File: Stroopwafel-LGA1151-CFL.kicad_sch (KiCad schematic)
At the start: 0 parts

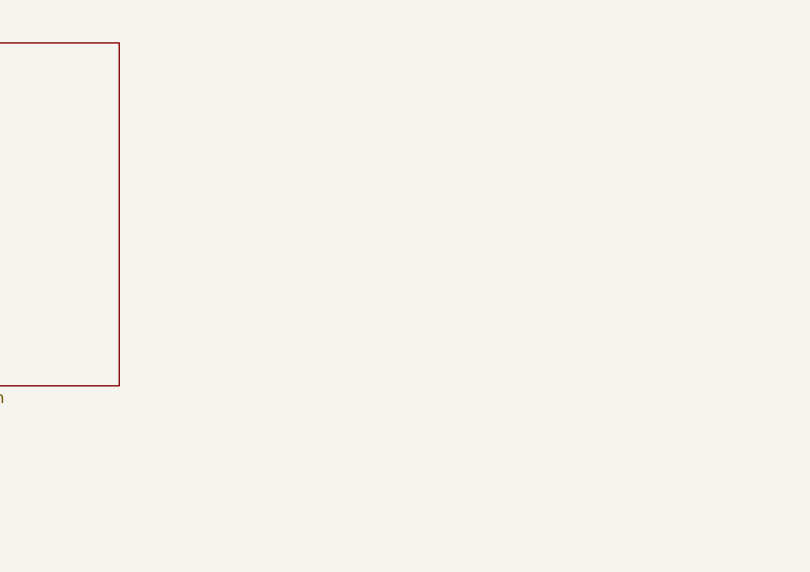
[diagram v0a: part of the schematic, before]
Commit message: Added CPU DDI symbol
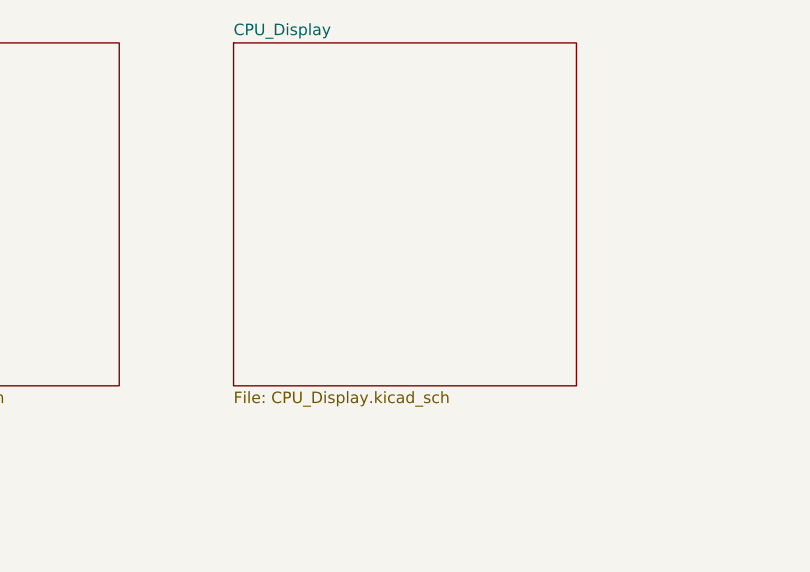
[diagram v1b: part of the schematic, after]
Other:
- added sheet CPU_Display (CPU_Display.kicad_sch)
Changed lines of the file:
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@@
+		)
+	)
+	(sheet
+		(at 177.8 76.2)
+		(size 38.1 38.1)
+		(exclude_from_sim no)
+		(in_bom yes)
+		(on_board yes)
+		(dnp no)
+		(fields_autoplaced yes)
+		(stroke
+			(width 0.1524)
+			(type solid)
+		)
+		(fill
+			(color 0 0 0 0.0000)
+		)
+		(property "Sheetname" "CPU_Display"
+			(at 177.8 75.4884 0)
+			(effects
+				(font
+					(size 1.27 1.27)
+				)
+				(justify left bottom)
+			)
+		)
+		(property "Sheetfile" "CPU_Display.kicad_sch"
+			(at 177.8 114.8846 0)
+			(effects
+				(font
+					(size 1.27 1.27)
+				)
+				(justify left top)
+			)
+		)
+		(instances
+			(project "Stroopwafel-LGA1151-CFL"
+				(path "/4bc771b8-eb19-46d0-8798-27231a7c6e83"
+					(page "4")
+				)
+			)
 		)
 	)

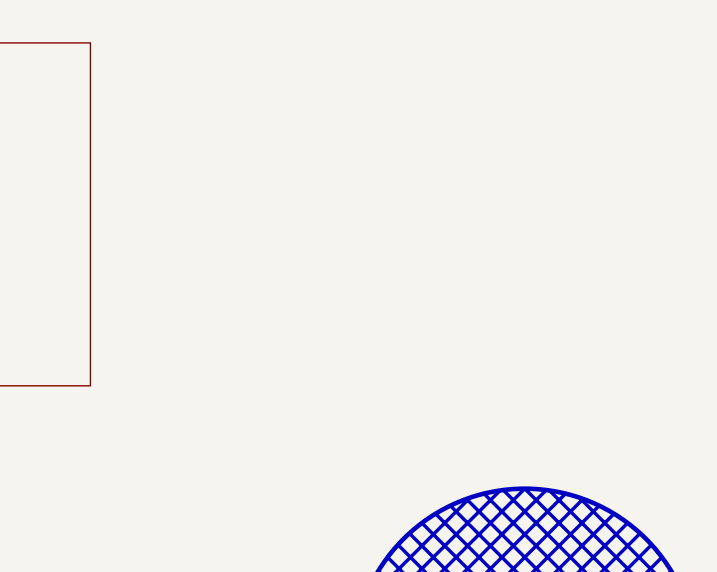
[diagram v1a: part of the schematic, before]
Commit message: Added CPU clock/cfg/vid/jtag symbol
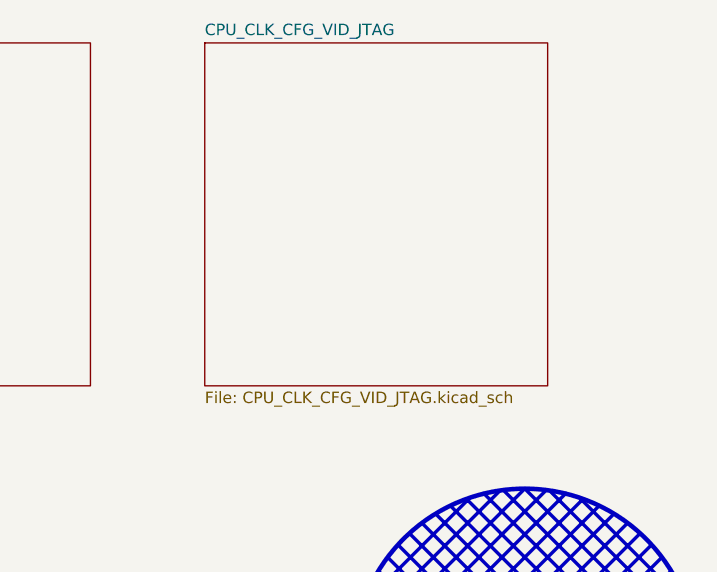
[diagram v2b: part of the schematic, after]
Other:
- added sheet CPU_CLK_CFG_VID_JTAG (CPU_CLK_CFG_VID_JTAG.kicad_sch)
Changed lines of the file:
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@@
+	)
+	(sheet
+		(at 228.6 76.2)
+		(size 38.1 38.1)
+		(exclude_from_sim no)
+		(in_bom yes)
+		(on_board yes)
+		(dnp no)
+		(fields_autoplaced yes)
+		(stroke
+			(width 0.1524)
+			(type solid)
+		)
+		(fill
+			(color 0 0 0 0.0000)
+		)
+		(property "Sheetname" "CPU_CLK_CFG_VID_JTAG"
+			(at 228.6 75.4884 0)
+			(effects
+				(font
+					(size 1.27 1.27)
+				)
+				(justify left bottom)
+			)
+		)
+		(property "Sheetfile" "CPU_CLK_CFG_VID_JTAG.kicad_sch"
+			(at 228.6 114.8846 0)
+			(effects
+				(font
+					(size 1.27 1.27)
+				)
+				(justify left top)
+			)
+		)
+		(instances
+			(project "Stroopwafel-LGA1151-CFL"
+				(path "/4bc771b8-eb19-46d0-8798-27231a7c6e83"
+					(page "5")
+				)
+			)
+		)
 	)
 	(sheet

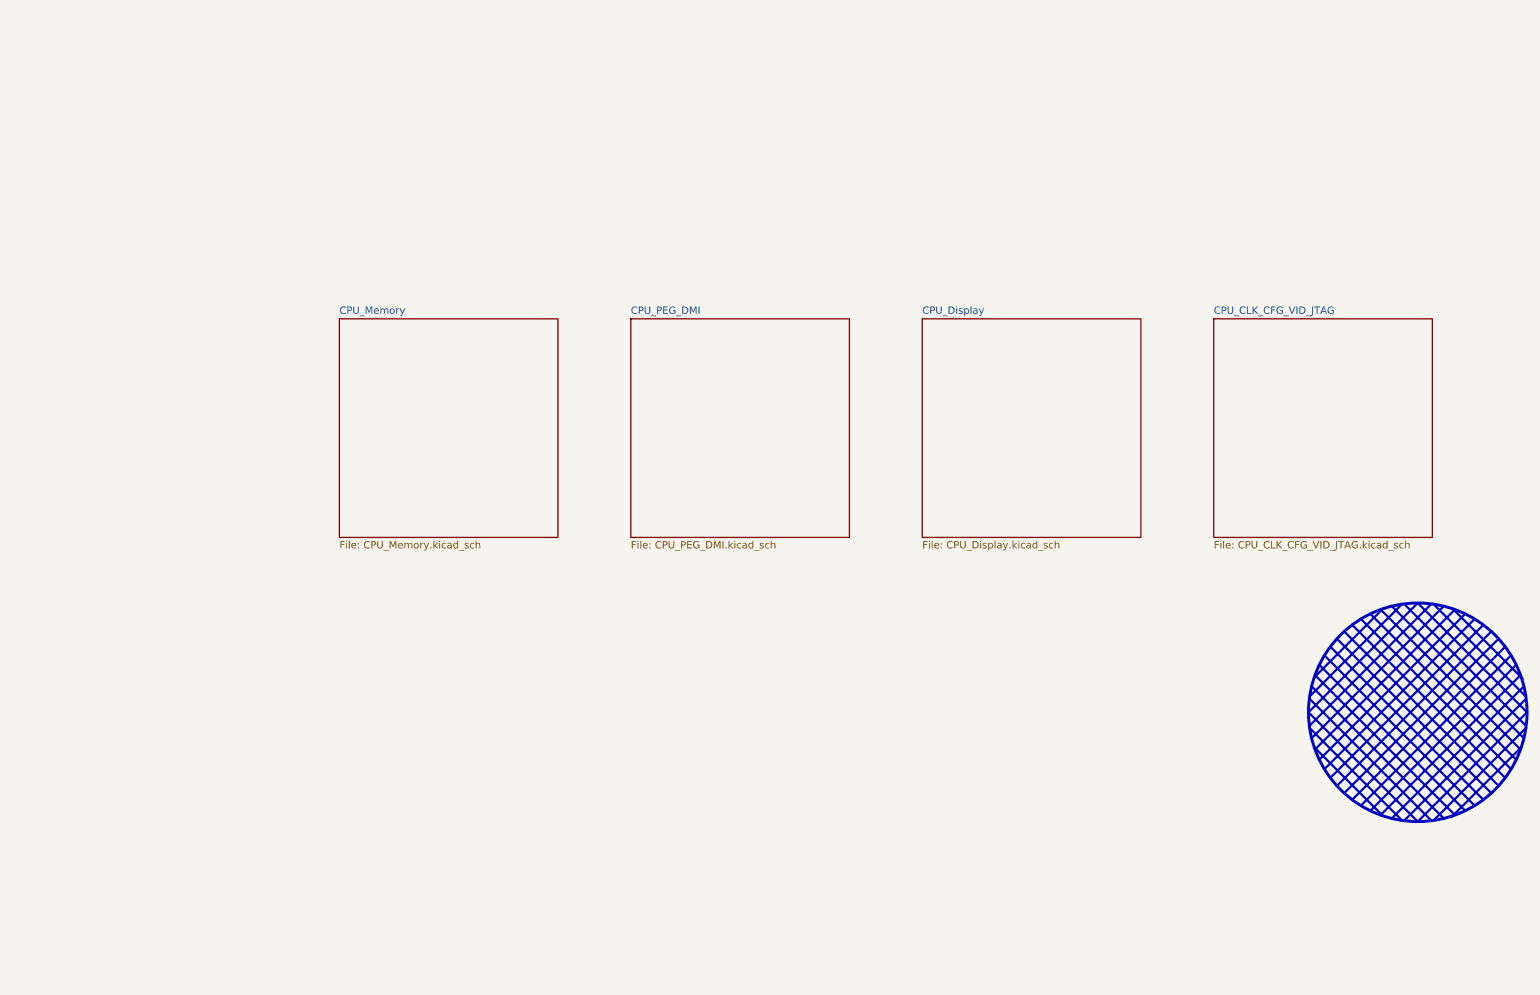
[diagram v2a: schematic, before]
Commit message: Added CPU GND and Core VCC symbols
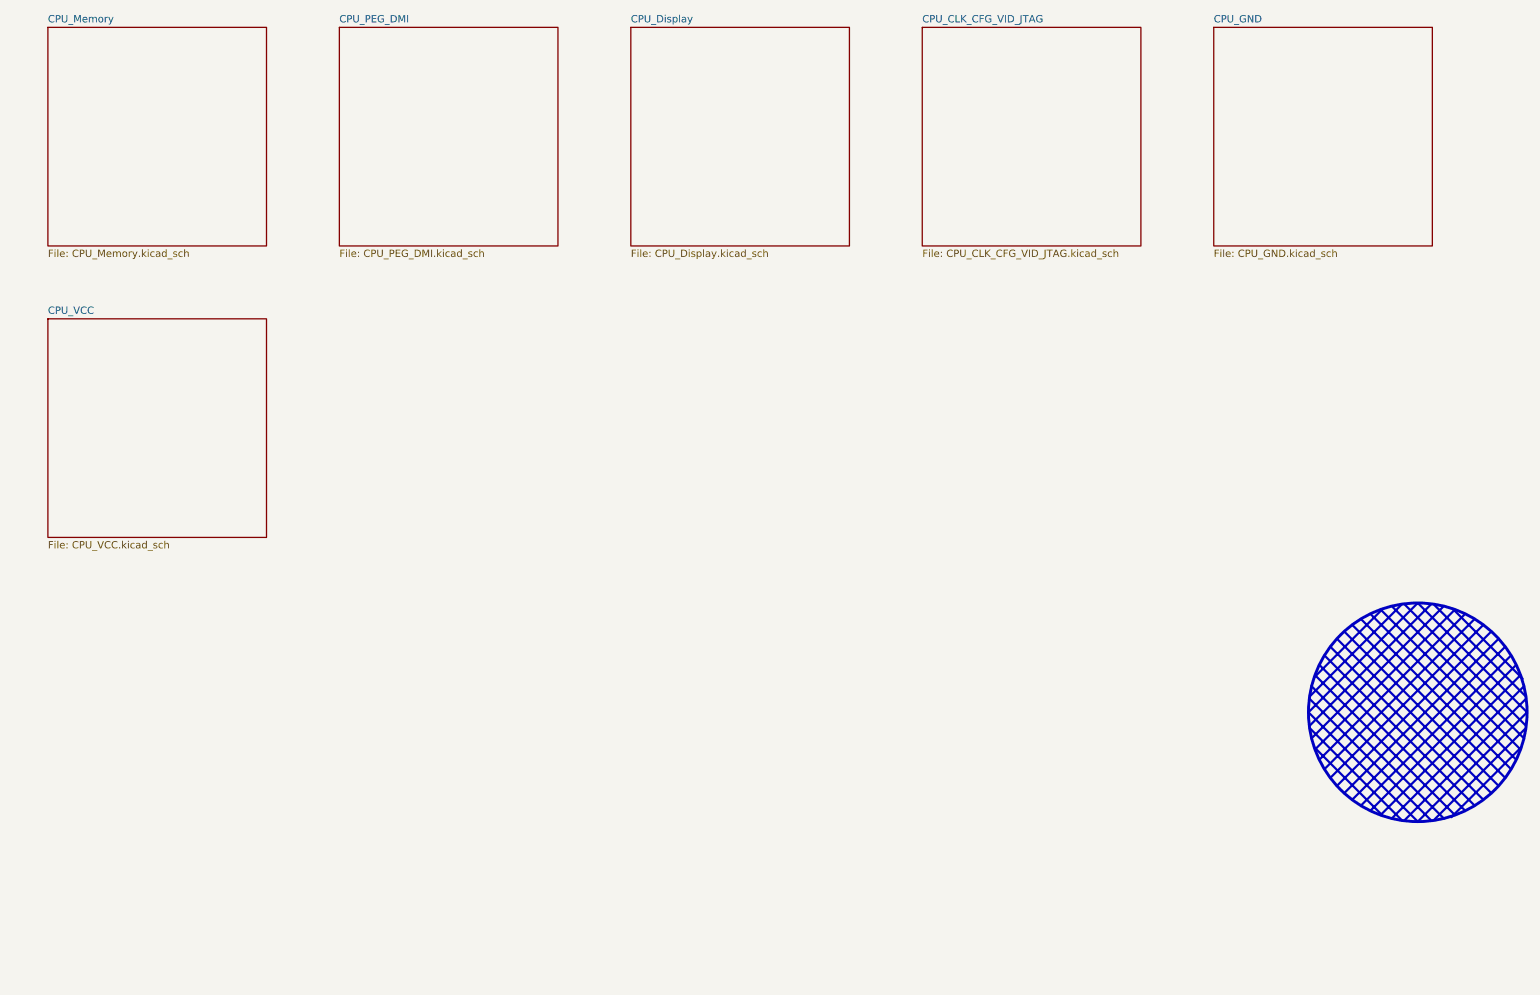
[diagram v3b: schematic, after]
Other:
- added sheet CPU_GND (CPU_GND.kicad_sch)
- added sheet CPU_VCC (CPU_VCC.kicad_sch)
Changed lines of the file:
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@@
 	)
 	(sheet
-		(at 127 76.2)
+		(at 76.2 25.4)
 		(size 38.1 38.1)
 		(exclude_from_sim no)
@@
 		)
 		(property "Sheetname" "CPU_PEG_DMI"
-			(at 127 75.4884 0)
+			(at 76.2 24.6884 0)
 			(effects
 				(font
@@
 		)
 		(property "Sheetfile" "CPU_PEG_DMI.kicad_sch"
-			(at 127 114.8846 0)
+			(at 76.2 64.0846 0)
 			(effects
 				(font
@@
 	)
 	(sheet
-		(at 228.6 76.2)
+		(at 177.8 25.4)
 		(size 38.1 38.1)
 		(exclude_from_sim no)
@@
 		)
 		(property "Sheetname" "CPU_CLK_CFG_VID_JTAG"
-			(at 228.6 75.4884 0)
+			(at 177.8 24.6884 0)
 			(effects
 				(font
@@
 		)
 		(property "Sheetfile" "CPU_CLK_CFG_VID_JTAG.kicad_sch"
-			(at 228.6 114.8846 0)
+			(at 177.8 64.0846 0)
 			(effects
 				(font
@@
 	)
 	(sheet
-		(at 76.2 76.2)
+		(at 25.4 76.2)
+		(size 38.1 38.1)
+		(exclude_from_sim no)
+		(in_bom yes)
+		(on_board yes)
+		(dnp no)
+		(fields_autoplaced yes)
+		(stroke
+			(width 0.1524)
+			(type solid)
+		)
+		(fill
+			(color 0 0 0 0.0000)
+		)
+		(property "Sheetname" "CPU_VCC"
+			(at 25.4 75.4884 0)
+			(effects
+				(font
+					(size 1.27 1.27)
+				)
+				(justify left bottom)
+			)
+		)
+		(property "Sheetfile" "CPU_VCC.kicad_sch"
+			(at 25.4 114.8846 0)
+			(effects
+				(font
+					(size 1.27 1.27)
+				)
+				(justify left top)
+			)
+		)
+		(instances
+			(project "Stroopwafel-LGA1151-CFL"
+				(path "/4bc771b8-eb19-46d0-8798-27231a7c6e83"
+					(page "7")
+				)
+			)
+		)
+	)
+	(sheet
+		(at 228.6 25.4)
+		(size 38.1 38.1)
+		(exclude_from_sim no)
+		(in_bom yes)
+		(on_board yes)
+		(dnp no)
+		(fields_autoplaced yes)
+		(stroke
+			(width 0.1524)
+			(type solid)
+		)
+		(fill
+			(color 0 0 0 0.0000)
+		)
+		(property "Sheetname" "CPU_GND"
+			(at 228.6 24.6884 0)
+			(effects
+				(font
+					(size 1.27 1.27)
+				)
+				(justify left bottom)
+			)
+		)
+		(property "Sheetfile" "CPU_GND.kicad_sch"
+			(at 228.6 64.0846 0)
+			(effects
+				(font
+					(size 1.27 1.27)
+				)
+				(justify left top)
+			)
+		)
+		(instances
+			(project "Stroopwafel-LGA1151-CFL"
+				(path "/4bc771b8-eb19-46d0-8798-27231a7c6e83"
+					(page "6")
+				)
+			)
+		)
+	)
+	(sheet
+		(at 25.4 25.4)
 		(size 38.1 38.1)
 		(exclude_from_sim no)
@@
 		)
 		(property "Sheetname" "CPU_Memory"
-			(at 76.2 75.4884 0)
+			(at 25.4 24.6884 0)
 			(effects
 				(font
@@
 		)
 		(property "Sheetfile" "CPU_Memory.kicad_sch"
-			(at 76.2 114.8846 0)
+			(at 25.4 64.0846 0)
 			(effects
 				(font
@@
 	)
 	(sheet
-		(at 177.8 76.2)
+		(at 127 25.4)
 		(size 38.1 38.1)
 		(exclude_from_sim no)
@@
 		)
 		(property "Sheetname" "CPU_Display"
-			(at 177.8 75.4884 0)
+			(at 127 24.6884 0)
 			(effects
 				(font
@@
 		)
 		(property "Sheetfile" "CPU_Display.kicad_sch"
-			(at 177.8 114.8846 0)
-			(effects
-				(font
+			(at 127 64.0846 0)
+			(effects
+				(font

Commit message: Added CPU Misc & RSVD symbol
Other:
- added sheet CPU_Misc (CPU_Misc.kicad_sch)
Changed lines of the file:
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@@
+	)
+	(sheet
+		(at 76.2 76.2)
+		(size 38.1 38.1)
+		(exclude_from_sim no)
+		(in_bom yes)
+		(on_board yes)
+		(dnp no)
+		(fields_autoplaced yes)
+		(stroke
+			(width 0.1524)
+			(type solid)
+		)
+		(fill
+			(color 0 0 0 0.0000)
+		)
+		(property "Sheetname" "CPU_Misc"
+			(at 76.2 75.4884 0)
+			(effects
+				(font
+					(size 1.27 1.27)
+				)
+				(justify left bottom)
+			)
+		)
+		(property "Sheetfile" "CPU_Misc.kicad_sch"
+			(at 76.2 114.8846 0)
+			(effects
+				(font
+					(size 1.27 1.27)
+				)
+				(justify left top)
+			)
+		)
+		(instances
+			(project "Stroopwafel-LGA1151-CFL"
+				(path "/4bc771b8-eb19-46d0-8798-27231a7c6e83"
+					(page "8")
+				)
+			)
+		)
 	)
 	(sheet

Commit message: Added first PCH symbol and footprint
THANKS @mothenjoyer69 so much for extracting and converting the PCH footprint from a laptop boardview ❤️
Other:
- added sheet PCH_SPI_SML_GSX (PCH_SPI_SML_GSX.kicad_sch)
- note added: "Stroopwafel LGA 1151 Intel Coffee Lake motherboard project by WifiCable"
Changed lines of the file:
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@@
 		(title "Stroopwafel LGA1151 CFL")
 		(company "WifiCable")
+		(comment 1 "WCFC WC-B551")
 		(comment 3 "stroopwafel for your coffee (lake)")
 	)
@@
 		(fill
 			(type none)
+		)
+	)
+	(text "Stroopwafel LGA 1151\nIntel Coffee Lake motherboard project\nby WifiCable"
+		(exclude_from_sim no)
+		(at 19.05 167.64 0)
+		(effects
+			(font
+				(size 5.08 5.08)
+				(thickness 1.016)
+				(bold yes)
+				(color 212 35 8 1)
+			)
+			(justify left top)
 		)
 	)
@@
 				)
 			)
+		)
+	)
+	(sheet
+		(at 127 76.2)
+		(size 38.1 38.1)
+		(exclude_from_sim no)
+		(in_bom yes)
+		(on_board yes)
+		(dnp no)
+		(fields_autoplaced yes)
+		(stroke
+			(width 0.1524)
+			(type solid)
+		)
+		(fill
+			(color 0 0 0 0.0000)
+		)
+		(property "Sheetname" "PCH_SPI_SML_GSX"
+			(at 127 75.4884 0)
+			(effects
+				(font
+					(size 1.27 1.27)
+				)
+				(justify left bottom)
+			)
+		)
+		(property "Sheetfile" "PCH_SPI_SML_GSX.kicad_sch"
+			(at 127 114.8846 0)
+			(effects
+				(font
+					(size 1.27 1.27)
+				)
+				(justify left top)
+			)
+		)
+		(instances
+			(project "Stroopwafel-LGA1151-CFL"
+				(path "/4bc771b8-eb19-46d0-8798-27231a7c6e83"
+					(page "9")
+				)
+			)

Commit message: Added all the PCH symbols
that took 1.5 days straight lol
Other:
- removed sheet PCH_SPI_SML_GSX
- added sheet PCH_temp (PCH_temp.kicad_sch)
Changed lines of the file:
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@@
+	)
+	(sheet
+		(at 127 76.2)
+		(size 38.1 38.1)
+		(exclude_from_sim no)
+		(in_bom yes)
+		(on_board yes)
+		(dnp no)
+		(fields_autoplaced yes)
+		(stroke
+			(width 0.1524)
+			(type solid)
+		)
+		(fill
+			(color 0 0 0 0.0000)
+		)
+		(property "Sheetname" "PCH_temp"
+			(at 127 75.4884 0)
+			(effects
+				(font
+					(size 1.27 1.27)
+				)
+				(justify left bottom)
+			)
+		)
+		(property "Sheetfile" "PCH_temp.kicad_sch"
+			(at 127 114.8846 0)
+			(effects
+				(font
+					(size 1.27 1.27)
+				)
+				(justify left top)
+			)
+		)
+		(instances
+			(project "Stroopwafel-LGA1151-CFL"
+				(path "/4bc771b8-eb19-46d0-8798-27231a7c6e83"
+					(page "9")
+				)
+			)
+		)
 	)
 	(sheet
@@
 				)
 			)
-		)
-	)
-	(sheet
-		(at 127 76.2)
-		(size 38.1 38.1)
-		(exclude_from_sim no)
-		(in_bom yes)
-		(on_board yes)
-		(dnp no)
-		(fields_autoplaced yes)
-		(stroke
-			(width 0.1524)
-			(type solid)
-		)
-		(fill
-			(color 0 0 0 0.0000)
-		)
-		(property "Sheetname" "PCH_SPI_SML_GSX"
-			(at 127 75.4884 0)
-			(effects
-				(font
-					(size 1.27 1.27)
-				)
-				(justify left bottom)
-			)
-		)
-		(property "Sheetfile" "PCH_SPI_SML_GSX.kicad_sch"
-			(at 127 114.8846 0)
-			(effects
-				(font
-					(size 1.27 1.27)
-				)
-				(justify left top)
-			)
-		)
-		(instances
-			(project "Stroopwafel-LGA1151-CFL"
-				(path "/4bc771b8-eb19-46d0-8798-27231a7c6e83"
-					(page "9")
-				)
-			)
